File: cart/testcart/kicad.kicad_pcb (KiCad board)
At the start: 4 copper layers, 100 x 78.5 mm, 16 parts, among them J1 Bus_TI994A_Cart, J2 Conn_01x06, U1 MCP1700-3302E_TO92, U3 GigaCart_CPLD_LC4064, U5 DIP-42_W15.24mm_Socket, U6 Pin_Header_Straight_2x05_Pitc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

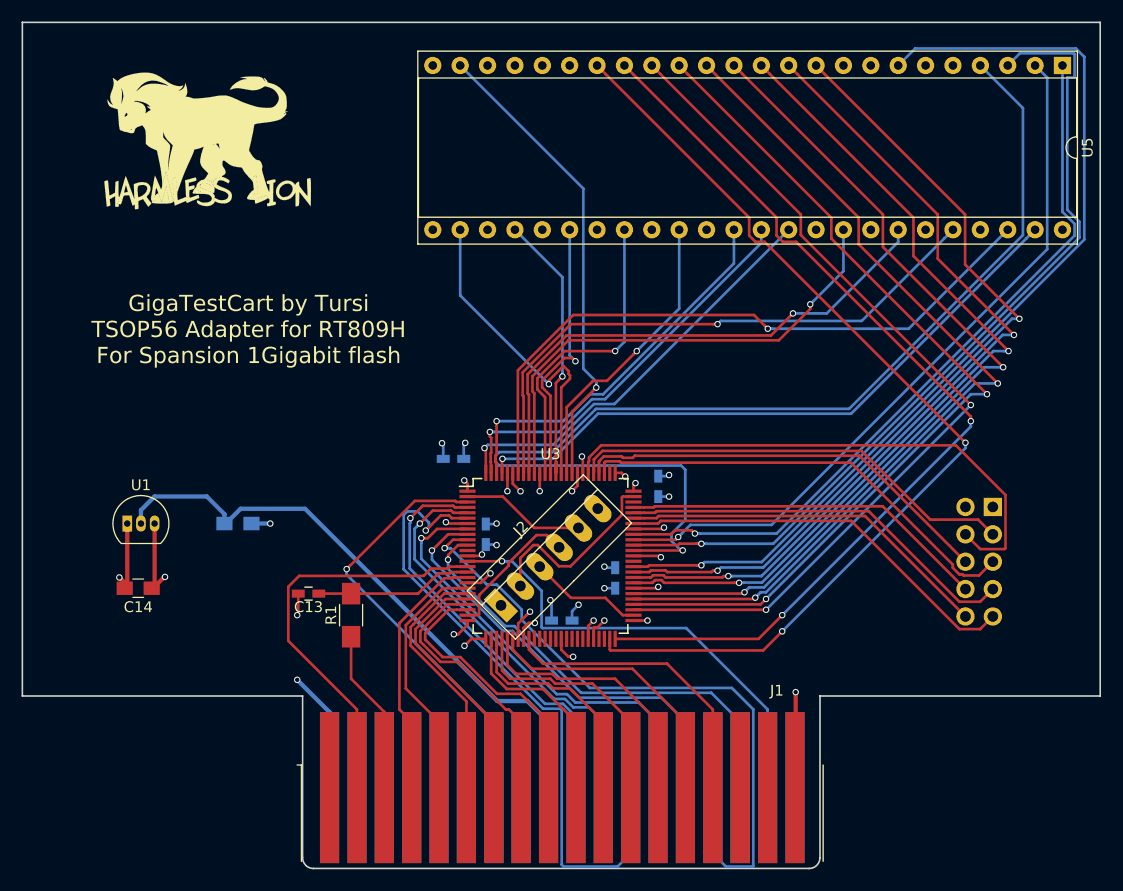
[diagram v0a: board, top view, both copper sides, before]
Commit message: forgot I was using git on this project... ahem. current state: CPLD operates, ROM works, GROM works without autoincrement. Autoinc is breaking the TI and not sure why!
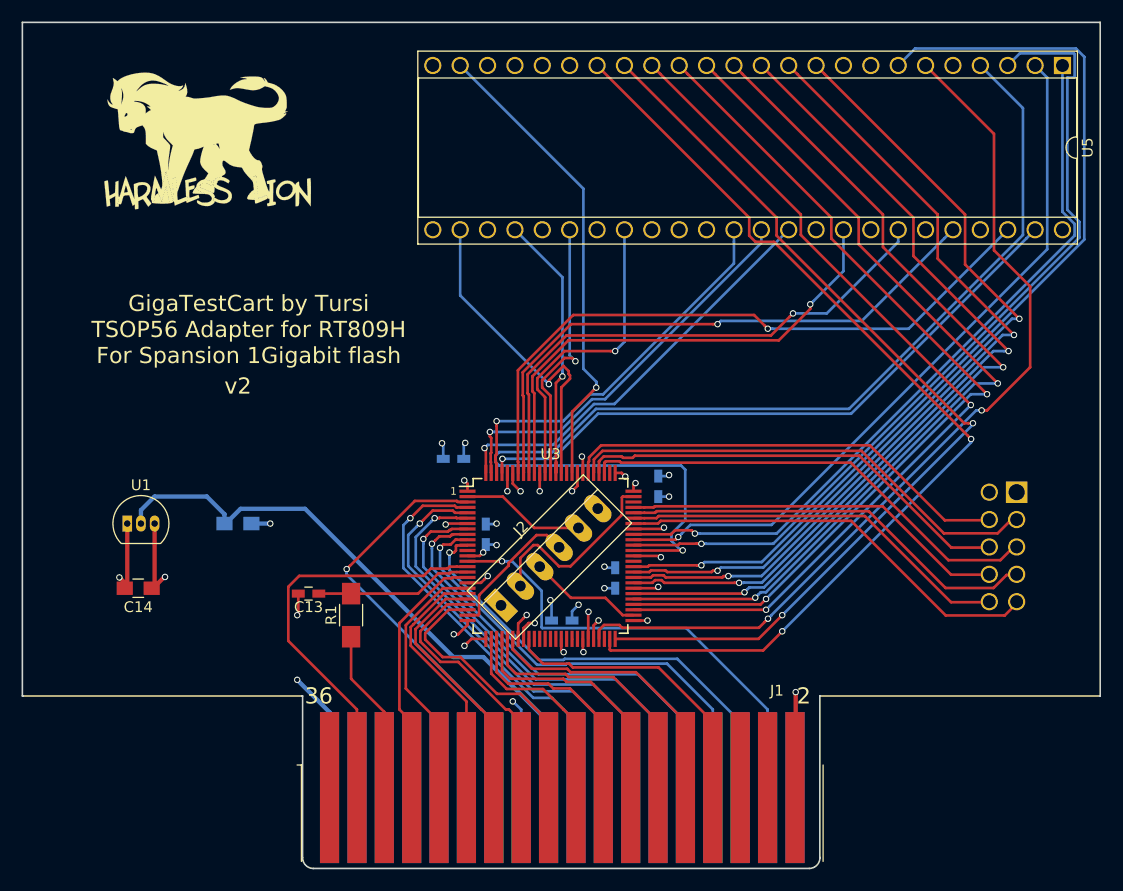
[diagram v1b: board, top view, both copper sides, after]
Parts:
- moved U6 2.60 mm to (184.8, 100.6)
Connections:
- U3 pad 44: Net-(J6-Pad1) -> Net-(J1-Pad21)
- U5 pad 34: Net-(U2-Pad34) -> GND
- U5 pad 6: +3V3 -> (no net)
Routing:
- net (no net): track 0.00 -> 83.2 mm, vias 0 -> 2
- net Net-(U2-Pad34): track 27.6 -> 0.00 mm, vias 1 -> 0
- net Net-(J1-Pad21): track 0.00 -> 18.1 mm, vias 0 -> 2
- net TI_D2: track 60.9 -> 46.4 mm
- net TI_D5: track 62.8 -> 48.9 mm
- net Net-(U2-Pad1): track 51.7 -> 41.9 mm
- net Net-(U2-Pad2): track 41.8 -> 44.4 mm
- net Net-(U2-Pad8): track 38.1 -> 39.9 mm
- net Net-(U2-Pad5): track 34.0 -> 35.8 mm
- net Net-(U2-Pad3): track 39.5 -> 41.2 mm
- net Net-(U2-Pad7): track 34.7 -> 36.4 mm
- net Net-(U2-Pad6): track 37.4 -> 39.0 mm
- net Net-(U2-Pad4): track 42.1 -> 43.6 mm
- net TI_D1: track 38.4 -> 39.6 mm
- net GND: track 61.9 -> 60.7 mm
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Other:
- board text added: "1"
- board text added: "2"
- board text added: "35"
- board text added: "36"
- board text added: "JTAG.Hdr 6 3v3 5 TDI 4 TCK 3 TMS 2 TDO 1 GND"
- board text added: "v2"
- board text removed: "JTAG.Hdr 1 GND 2 TDO 3 TMS 4 TCK 5 TDI 6 3v3"

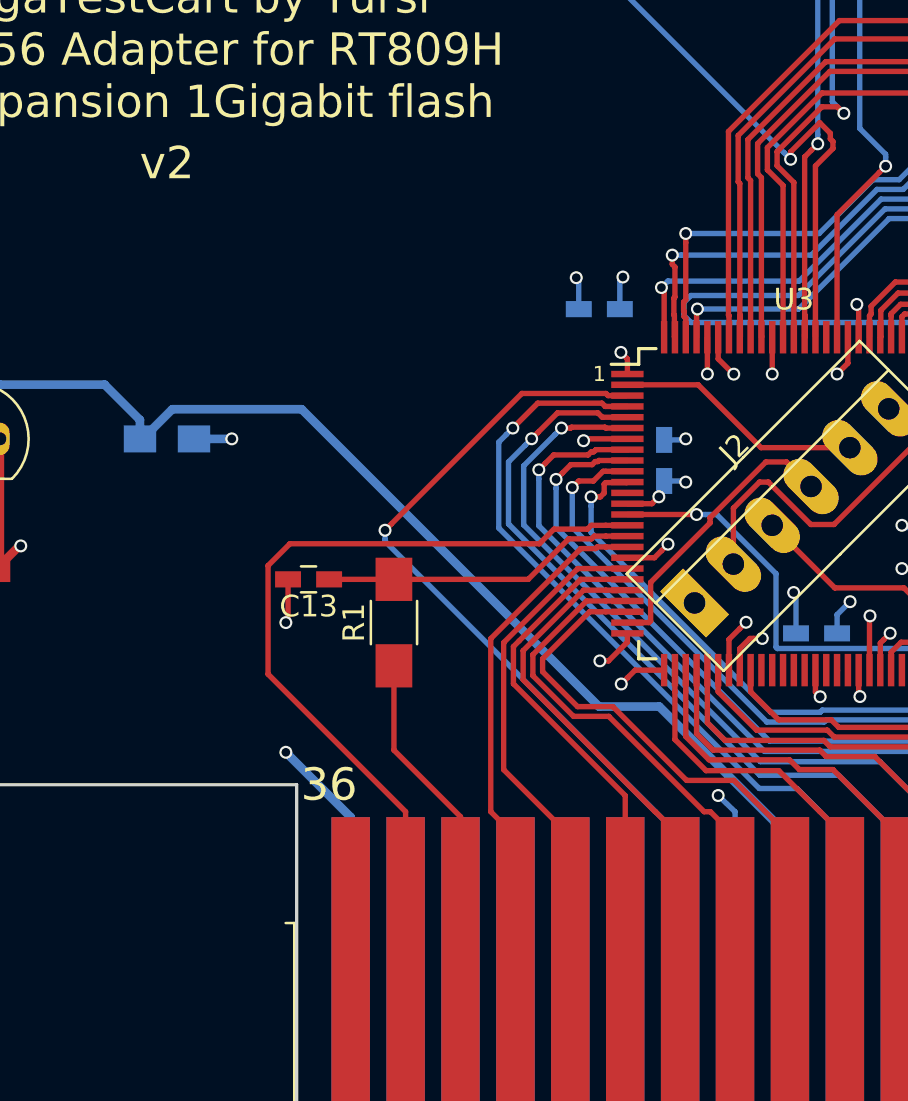
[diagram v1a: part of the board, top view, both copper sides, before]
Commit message: Updated reset mechanism on CPLD to be tied to GROM selection. A bit hacky, but it appears to work better.
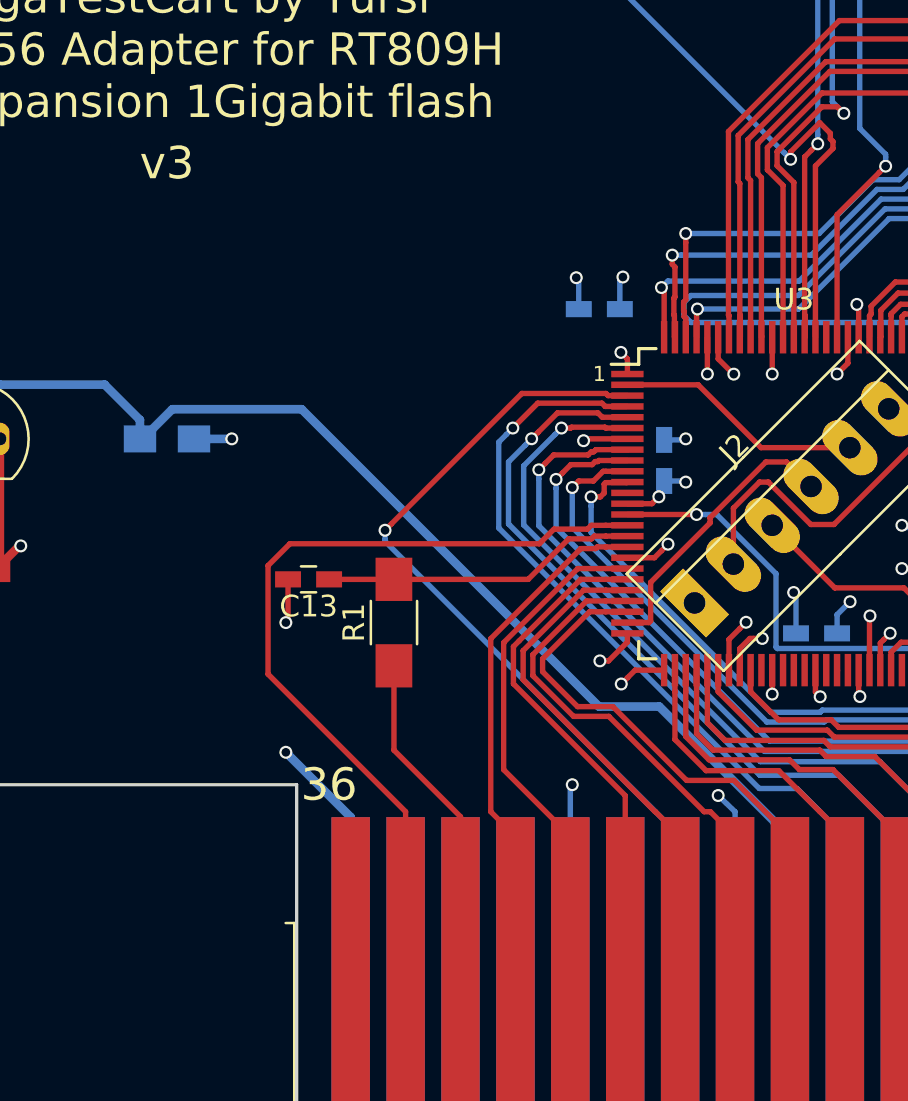
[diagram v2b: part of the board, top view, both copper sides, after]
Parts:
- R1: value 68^ -> 47^
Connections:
- net Net-(J1-Pad21) renamed TI_GSEL
- J1 pad 27: Net-(J1-Pad27) -> TI_GCLK
- U3 pad 36: (no net) -> TI_GCLK
- U3 pad 47: (no net) -> Net-(U2-Pad14)
- U3 pad 48: (no net) -> Net-(J6-Pad1)
- U3 pad 85: Net-(U2-Pad34) -> (no net)
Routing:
- net Net-(U2-Pad14): track 0.00 -> 83.2 mm, vias 0 -> 2
- net (no net): track 83.2 -> 0.00 mm, vias 2 -> 0
- net TI_GCLK: track 0.00 -> 20.6 mm, vias 0 -> 2
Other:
- board text added: "v3"
- board text removed: "v2"
